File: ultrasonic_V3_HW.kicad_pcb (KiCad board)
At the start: 4 copper layers, 130 x 100 mm, 252 parts, among them J1 71918-140LF, J2 Conn_Coaxial, J3 Conn_Coaxial, J4 Conn_01x07_Pin, J5 Screw_Terminal_01x02, J6 Conn_Coaxial, J7 Conn_Coaxial, Q1 DMN6069SE, Q10 DMN6069SE, Q11 DMN6069SE, Q12 Q_NMOS_GSD, Q2 DMN6069SE, Q3 DMN6069SE, Q4 DMN6069SE, Q5 Q_NMOS_GSD, Q6 Q_NMOS_GSD, Q7 DMN6069SE, Q8 DMN6069SE, Q9 DMN6069SE, U1 MACHXO2-1200HC-4TG100C, U10 MIC4604YM, U11 MIC4604YM, U12 OKI-78SR-3.3_1.5-W36H-C, U13 OKI-78SR-12_1.0-W36H-C, U15 LM34966, U17 OPA388, U18 LM393, U19 TMUX7219, U2 TDC_7200, U20 TMUX7219, U21 TMUX7219, U22 TMUX7219, U23 MCP1501-25xCH, U24 MCP1501-30xCH, U3 MAX9939, U4 TLV3501AID, U5 DAC60501, U6 LM339, U7 ADC10065, U8 MIC4604YM, U9 MIC4604YM, X1 16MHz

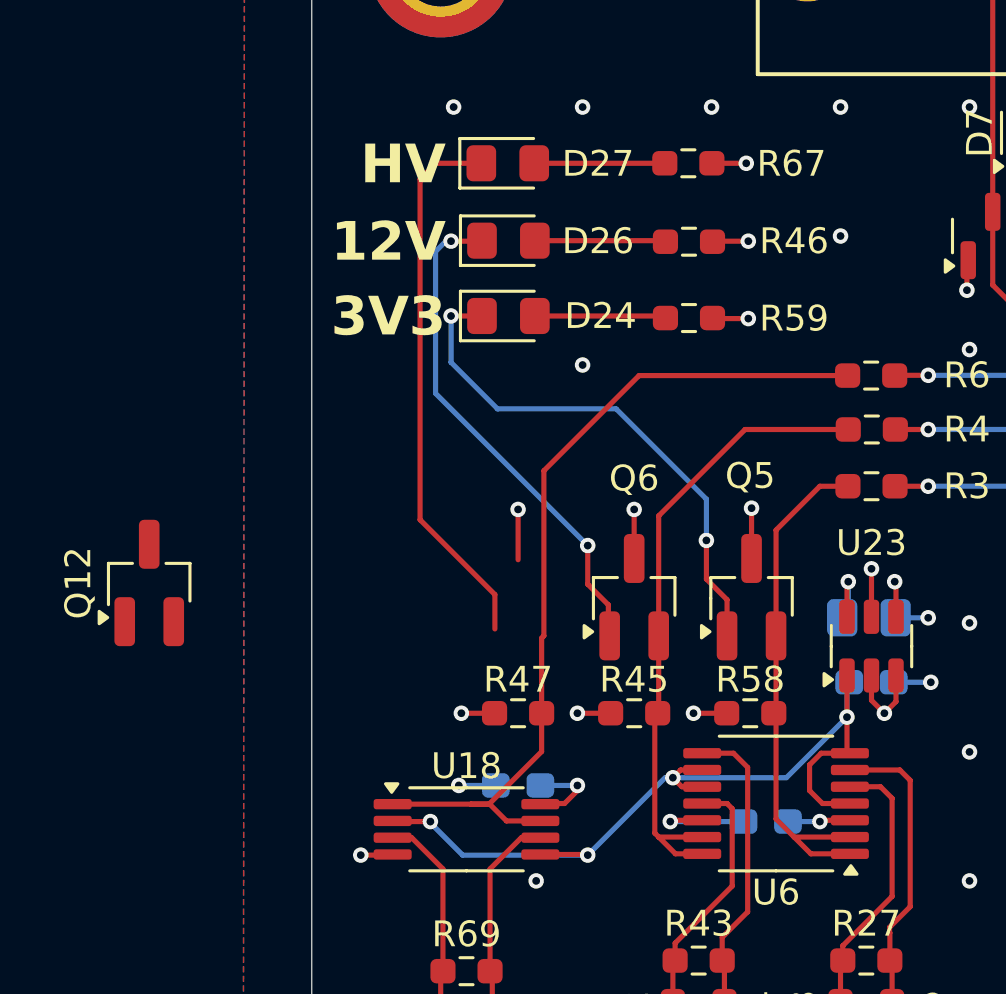
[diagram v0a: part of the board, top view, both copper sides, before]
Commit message: V1 completed, starting on V2 after consultation with mr. Chalupa
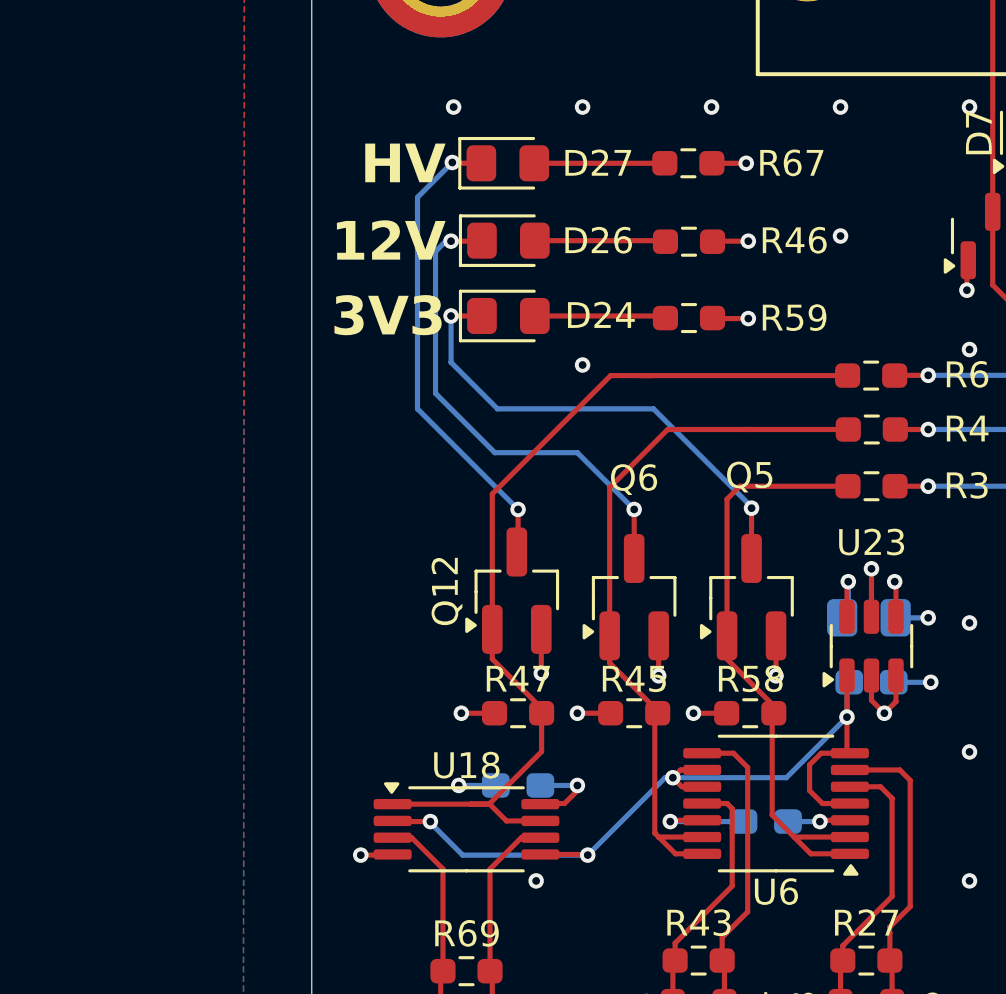
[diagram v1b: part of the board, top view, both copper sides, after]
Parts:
- C3, C34: value C -> 100n
- C35: value C -> 10n
- C36: value C -> 1u
- R62, R63, R64, R65: value R -> 100
- R66: value R -> 6k8
- R71: value R -> 4k7
- moved Q12 14.3 mm to (92.5, 73.8)
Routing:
- net /P_GOOD_P12V: track 25.0 -> 28.5 mm
- net /P_GOOD_P3V3: track 20.3 -> 23.7 mm
- net Net-(D24-K): track 22.4 -> 19.0 mm, vias 3 -> 2
- net GND: track 227.0 -> 229.9 mm, vias 391 -> 393
- net /P_GOOD_PHV: track 33.8 -> 36.5 mm
- net Net-(D27-K): track 21.3 -> 18.7 mm, vias 0 -> 2
- net Net-(D26-K): track 21.3 -> 19.0 mm, vias 3 -> 2

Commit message: V2 finished
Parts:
- removed D10, D11, D12, D13, D15, D8, D9: BAT54S, Package_TO_SOT_SMD:SOT-23
- removed D7: BAT54S, Package_TO_SOT_SMD:SOT-23-3
- removed R85: 12, Resistor_SMD:R_0603_1608Metric
- added C100: 200p, Capacitor_SMD:C_0603_1608Metric_Pad1.08x0.95mm_HandSolder, F.Cu at (185.0, 95.3)
- added C101: 1n, Capacitor_SMD:C_0603_1608Metric_Pad1.08x0.95mm_HandSolder, F.Cu at (158.4, 108.8)
- added C102: 2u2, Capacitor_SMD:C_0805_2012Metric_Pad1.18x1.45mm_HandSolder, F.Cu at (168.8, 107.8)
- added C103: 100n, Capacitor_SMD:C_0603_1608Metric_Pad1.08x0.95mm_HandSolder, F.Cu at (170.7, 107.7)
- added C104: 2u2, Capacitor_SMD:C_0805_2012Metric_Pad1.18x1.45mm_HandSolder, F.Cu at (160.5, 112.7)
- added C105: 100n, Capacitor_SMD:C_0603_1608Metric_Pad1.08x0.95mm_HandSolder, F.Cu at (160.7, 110.5)
- added C106: C, Capacitor_SMD:C_0603_1608Metric_Pad1.08x0.95mm_HandSolder, F.Cu at (169.5, 93.3)
- added C107: C, Capacitor_SMD:C_0603_1608Metric_Pad1.08x0.95mm_HandSolder, F.Cu at (169.5, 94.8)
- added C108: C, Capacitor_SMD:C_0603_1608Metric_Pad1.08x0.95mm_HandSolder, B.Cu at (148.7, 104.6)
- added C109: C, Capacitor_SMD:C_0805_2012Metric_Pad1.18x1.45mm_HandSolder, B.Cu at (145.8, 93.4)
- added C110: 100n, Capacitor_SMD:C_0603_1608Metric_Pad1.08x0.95mm_HandSolder, B.Cu at (164.6, 90.5)
- added C111: C, Capacitor_SMD:C_0603_1608Metric_Pad1.08x0.95mm_HandSolder, B.Cu at (132.3, 84.1)
- added C112: C, Capacitor_SMD:C_0603_1608Metric_Pad1.08x0.95mm_HandSolder, B.Cu at (130.9, 102.3)
- added C113: 100n, Capacitor_SMD:C_0603_1608Metric_Pad1.08x0.95mm_HandSolder, F.Cu at (122.8, 127.2)
- added C114: 10u, Capacitor_SMD:C_0805_2012Metric_Pad1.18x1.45mm_HandSolder, F.Cu at (116.8, 125.3)
- added C115: 10u, Capacitor_SMD:C_0805_2012Metric_Pad1.18x1.45mm_HandSolder, F.Cu at (116.8, 123.3)
- added C116: 100n, Capacitor_SMD:C_0603_1608Metric_Pad1.08x0.95mm_HandSolder, F.Cu at (113.2, 125.6)
- added C117: 100n, Capacitor_SMD:C_0603_1608Metric_Pad1.08x0.95mm_HandSolder, F.Cu at (113.2, 124.1)
- added C118: C, Capacitor_SMD:C_0603_1608Metric_Pad1.08x0.95mm_HandSolder, B.Cu at (181.1, 115.7)
- added C119: C, Capacitor_SMD:C_0603_1608Metric_Pad1.08x0.95mm_HandSolder, B.Cu at (200.8, 114.0)
- added C120: C, Capacitor_SMD:C_0805_2012Metric_Pad1.18x1.45mm_HandSolder, B.Cu at (202.8, 113.8)
- added C121: C, Capacitor_SMD:C_0805_2012Metric_Pad1.18x1.45mm_HandSolder, B.Cu at (183.1, 115.8)
- added C122: C, Capacitor_SMD:C_0603_1608Metric_Pad1.08x0.95mm_HandSolder, B.Cu at (192.7, 72.9)
- added C123: C, Capacitor_SMD:C_0603_1608Metric_Pad1.08x0.95mm_HandSolder, B.Cu at (202.1, 74.7)
- added C124: C, Capacitor_SMD:C_0805_2012Metric_Pad1.18x1.45mm_HandSolder, B.Cu at (191.0, 72.7)
- added C125: C, Capacitor_SMD:C_0805_2012Metric_Pad1.18x1.45mm_HandSolder, B.Cu at (200.1, 74.9)
- added C2: C, Capacitor_SMD:C_0603_1608Metric_Pad1.08x0.95mm_HandSolder, B.Cu at (202.8, 69.5)
- added C90: C, Capacitor_SMD:C_0603_1608Metric_Pad1.08x0.95mm_HandSolder, B.Cu at (203.0, 121.0)
- added C91: C, Capacitor_SMD:C_0805_2012Metric_Pad1.18x1.45mm_HandSolder, B.Cu at (207.0, 119.0)
- added C92: C, Capacitor_SMD:C_0603_1608Metric_Pad1.08x0.95mm_HandSolder, B.Cu at (183.3, 121.0)
- added C93: C, Capacitor_SMD:C_0805_2012Metric_Pad1.18x1.45mm_HandSolder, B.Cu at (187.4, 121.1)
- added C94: 10u, Capacitor_SMD:C_0805_2012Metric_Pad1.18x1.45mm_HandSolder, F.Cu at (122.8, 130.9)
- added C95: 10u, Capacitor_SMD:C_0805_2012Metric_Pad1.18x1.45mm_HandSolder, F.Cu at (120.8, 130.9)
- added C96: 100n, Capacitor_SMD:C_0603_1608Metric_Pad1.08x0.95mm_HandSolder, F.Cu at (120.8, 127.2)
- added C97: 200p, Capacitor_SMD:C_0603_1608Metric_Pad1.08x0.95mm_HandSolder, F.Cu at (188.4, 98.8)
- added C98: 200p, Capacitor_SMD:C_0603_1608Metric_Pad1.08x0.95mm_HandSolder, F.Cu at (188.4, 89.9)
- added C99: 200p, Capacitor_SMD:C_0603_1608Metric_Pad1.08x0.95mm_HandSolder, F.Cu at (185.0, 93.8)
- added D28: SML4740A-E3/61, Diode_SMD:D_SMA_Handsoldering, F.Cu at (105.8, 124.5)
- added FB1: BLM21BD601SN1D, Resistor_SMD:R_0805_2012Metric_Pad1.20x1.40mm_HandSolder, B.Cu at (149.1, 92.4)
- added FB2: BLM21BD601SN1D, Resistor_SMD:R_0805_2012Metric_Pad1.20x1.40mm_HandSolder, B.Cu at (143.9, 85.5)
- added FB3: BLM21BD601SN1D, Resistor_SMD:R_0805_2012Metric_Pad1.20x1.40mm_HandSolder, B.Cu at (131.8, 105.2)
- added FB4: BLM21BD601SN1D, Resistor_SMD:R_0805_2012Metric_Pad1.20x1.40mm_HandSolder, B.Cu at (127.5, 101.4)
- added FB5: BLM21BD601SN1D, Resistor_SMD:R_0805_2012Metric_Pad1.20x1.40mm_HandSolder, B.Cu at (126.5, 95.5)
- added FB6: BLM21BD601SN1D, Resistor_SMD:R_0805_2012Metric_Pad1.20x1.40mm_HandSolder, B.Cu at (127.0, 90.4)
- added Q14: Q_PMOS_DGS, Package_TO_SOT_SMD:SOT-223-3_TabPin2, F.Cu at (105.9, 131.5)
- added R86: 200k, Resistor_SMD:R_0603_1608Metric_Pad0.98x0.95mm_HandSolder, B.Cu at (185.1, 95.3)
- added R87: R, Resistor_SMD:R_0603_1608Metric_Pad0.98x0.95mm_HandSolder, F.Cu at (169.5, 96.3)
- added R88: R, Capacitor_SMD:C_0603_1608Metric_Pad1.08x0.95mm_HandSolder, B.Cu at (143.8, 79.8)
- added U14: THS4521IDGK, Package_SO:VSSOP-8_3.0x3.0mm_P0.65mm, F.Cu at (188.5, 94.4)
- added U25: ADP7142ARDZ-3.3, Package_SO:SOIC-8-1EP_3.9x4.9mm_P1.27mm_EP2.29x3mm, F.Cu at (164.0, 107.0)
- added U26: USBLC6-2SC6, Package_TO_SOT_SMD:SOT-23-6, F.Cu at (122.1, 59.6)
- added U27: USBLC6-2SC6, Package_TO_SOT_SMD:SOT-23-6, F.Cu at (127.1, 59.6)
- added X2: LCMXO-7000HC-6TG-144C, Package_QFP:TQFP-144_20x20mm_P0.5mm, F.Cu at (140.8, 94.5)
- C1: value 100p -> 120p
- C10: value 1u -> C; moved to B.Cu
- C11: value 1u -> C; footprint Capacitor_SMD:C_0603_1608Metric_Pad1.08x0.95mm_HandSolder -> Capacitor_SMD:C_0805_2012Metric_Pad1.18x1.45mm_HandSolder; moved to B.Cu
- C12: value 100p -> 100n
- C14, C19, C23, C78, R83, R84: moved to F.Cu
- C24: value C -> 100p
- C44: footprint Capacitor_SMD:C_0603_1608Metric_Pad1.08x0.95mm_HandSolder -> Capacitor_SMD:C_0805_2012Metric_Pad1.18x1.45mm_HandSolder
- C53, C85: value 1u -> C; footprint Capacitor_SMD:C_0805_2012Metric_Pad1.18x1.45mm_HandSolder -> Capacitor_SMD:C_0603_1608Metric_Pad1.08x0.95mm_HandSolder
- C54: value 100n -> C
- C55: value 10n -> C
- C8: value C -> 120p
- C9: value 100n -> C; footprint Capacitor_SMD:C_0603_1608Metric_Pad1.08x0.95mm_HandSolder -> Capacitor_SMD:C_0805_2012Metric_Pad1.18x1.45mm_HandSolder
- F3, F4, R29: moved to B.Cu
- R14: value R -> 20
- R16: value 1k -> 10
- R17: value 1k -> 100k; footprint Resistor_SMD:R_0603_1608Metric_Pad0.98x0.95mm_HandSolder -> Resistor_SMD:R_1206_3216Metric_Pad1.30x1.75mm_HandSolder
- R18: value 0 -> 200k
- R19: value 1k -> 200k; moved to F.Cu
- R21: value 1k -> 10k; moved to F.Cu
- R23: value R -> 10k
- R60: value R -> 12; footprint Capacitor_SMD:C_0603_1608Metric_Pad1.08x0.95mm_HandSolder -> Resistor_SMD:R_0603_1608Metric; moved to F.Cu
- R7: value 10 -> 20
- R72: value 0 -> 200k; moved to B.Cu
- U1: value MACHXO2-1200HC-4TG100C -> USBLC6-2SC6; footprint Package_QFP:TQFP-100_14x14mm_P0.5mm -> Package_TO_SOT_SMD:SOT-23-6
- U17: value OPA388 -> NE5532; footprint Package_SO:VSSOP-8_3.0x3.0mm_P0.65mm -> Package_SO:SOIC-8_3.9x4.9mm_P1.27mm
- U24: value MCP1501-30xCH -> USBLC6-2SC6
- moved R17 72.3 mm to (101.7, 121.4)
- moved U24 56.1 mm to (111.9, 59.6), turned to -90 degrees
- moved C9 49.9 mm to (207.0, 67.5), turned to -90 degrees
- moved C85 46.1 mm to (138.5, 104.4), turned to 90 degrees
- moved R60 42.8 mm to (126.2, 90.3), turned to 0 degrees
- moved U1 41.5 mm to (117.0, 59.6), turned to -90 degrees
- moved C55 38.9 mm to (140.0, 104.4), turned to 90 degrees
- moved C11 32.8 mm to (187.0, 67.6)
- moved U17 29.5 mm to (196.6, 93.7), turned to 0 degrees
- moved C54 28.5 mm to (150.9, 100.9)
- moved C10 27.3 mm to (182.9, 69.5), turned to -90 degrees
- moved R21 23.4 mm to (192.1, 94.3), turned to 90 degrees
- moved R19 23.4 mm to (188.4, 88.4)
- moved C52 23.0 mm to (150.9, 85.7)
- moved C53 21.1 mm to (150.9, 88.7), turned to 180 degrees
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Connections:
- net Net-(U12-OUT) renamed /PowerManagement/P3V3_UNFUSED
- net Net-(U13-OUT) renamed /PowerManagement/P12V_UNFUSED
- C1 pad 2: Net-(U4-+) -> /AnalogFrontend/AMPLIFIED_SIGNAL_P
- C10 pad 1: Net-(U17A-+) -> /P12V
- C10 pad 2: /AnalogFrontend/AMPLIFIED_SIGNAL_P -> GND
- C11 pad 1: Net-(C11-Pad1) -> GND
- C11 pad 2: GND -> /P12V
- C12 pad 1: /AnalogFrontend/SIGNAL_UNAMPLIFIED_P -> GND
- C12 pad 2: /AnalogFrontend/SIGNAL_UNAMPLIFIED_N -> /P12V
- C13 pad 2: /P3V_REF -> /AnalogFrontend/P3V3_A
- C14 pad 1: /P3V3 -> /AnalogFrontend/P3V3_A
- C15 pad 2: /PHV -> /PowerManagement/step-up/PHV_UNFUSED
- C18 pad 2: /P3V3 -> /AnalogFrontend/P3V3_A
- C19 pad 2: /P3V3 -> /AnalogFrontend/P3V3_A
- C23 pad 2: Net-(U7-VCOM) -> /AnalogFrontend/Vcom
- C24 pad 2: /AnalogFrontend/AMPLIFIED_SIGNAL_P -> Net-(U4--)
- C37 pad 2: /P3V3 -> /fpga/fpgaBankPower/VCCIO0
- C38 pad 1: GND -> /fpga/fpgaBankPower/VCCIO1
- C38 pad 2: /P3V3 -> GND
- C39 pad 1: GND -> /fpga/fpgaBankPower/VCCIO2
- C39 pad 2: /P3V3 -> GND
- C40 pad 1: GND -> /fpga/fpgaBankPower/VCCIO3
- C40 pad 2: /P3V3 -> GND
- C41 pad 2: /P3V3 -> /fpga/fpgaBankPower/VCCIO4
- C42 pad 1: GND -> /fpga/fpgaBankPower/VCCIO5
- C42 pad 2: /P3V3 -> GND
- C43 pad 1: GND -> /fpga/fpgaBankPower/VCCIO0
- C43 pad 2: /P3V3 -> GND
- C44 pad 1: GND -> /P3V3
- C44 pad 2: /P3V3 -> GND
- C45 pad 2: /P3V3 -> /fpga/fpgaBankPower/VCCIO0
- C46 pad 1: GND -> /fpga/fpgaBankPower/VCCIO1
- C46 pad 2: /P3V3 -> GND
- C47 pad 1: GND -> /fpga/fpgaBankPower/VCCIO2
- C47 pad 2: /P3V3 -> GND
- C48 pad 1: GND -> /fpga/fpgaBankPower/VCCIO3
- C48 pad 2: /P3V3 -> GND
- C49 pad 1: GND -> /fpga/fpgaBankPower/VCCIO4
- C49 pad 2: /P3V3 -> GND
- C50 pad 1: GND -> /fpga/fpgaBankPower/VCCIO5
- C50 pad 2: /P3V3 -> GND
- C51 pad 1: GND -> /fpga/fpgaBankPower/VCCIO0
- C51 pad 2: /P3V3 -> GND
- C52 pad 1: GND -> /P3V3
- C52 pad 2: /P3V3 -> GND
- C53 pad 1: GND -> /fpga/fpgaBankPower/VCCIO1
- C53 pad 2: /P3V_REF -> GND
- C54 pad 1: /P3V_REF -> /fpga/fpgaBankPower/VCCIO1
- C55 pad 1: /P3V_REF -> /fpga/fpgaBankPower/VCCIO2
- C62 pad 2: /PHV -> /PowerManagement/step-up/PHV_UNFUSED
- C63 pad 1: /PHV -> /PowerManagement/step-up/PHV_UNFUSED
- C7 pad 2: /P3V3 -> /AnalogFrontend/P3V3_A
- C78 pad 1: /P3V3 -> /AnalogFrontend/P3V3_A
- C85 pad 1: /P3V3 -> /fpga/fpgaBankPower/VCCIO2
- C9 pad 1: /P3V3 -> GND
- C9 pad 2: GND -> /P12V
- F2 pad 1: /PowerManagement/P15V-20V_5S_UNREGULATED -> Net-(D28-K)
- J5 pad 1: /PowerManagement/P15V-20V_5S_UNREGULATED -> GND
- J5 pad 2: GND -> /PowerManagement/P15V-20V_5S_UNREGULATED
- R14 pad 2: Net-(U7-VIN-) -> Net-(U3A-OUTB)
- R15 pad 2: /P3V3 -> /AnalogFrontend/P3V3_A
- R16 pad 1: Net-(R16-Pad1) -> Net-(U4--)
- R16 pad 2: Net-(U17A--) -> /AnalogFrontend/DAC_COMPARATOR_REF
- R17 pad 1: Net-(C11-Pad1) -> GND
- R17 pad 2: Net-(U17A--) -> Net-(D28-A)
- R18 pad 1: /AnalogFrontend/AMPLIFIED_SIGNAL -> Net-(C100-Pad2)
- R18 pad 2: /AnalogFrontend/AMPLIFIED_SIGNAL_P -> /AnalogFrontend/SIGNAL_UNAMPLIFIED_N
- R19 pad 1: /P3V_REF -> Net-(C98-Pad1)
- R19 pad 2: Net-(U17A-+) -> /AnalogFrontend/SIGNAL_UNAMPLIFIED_P
- R21 pad 1: Net-(U17A-+) -> /AnalogFrontend/P3V3_A
- R21 pad 2: GND -> Net-(U17A-+)
- R22 pad 2: /P3V3 -> /AnalogFrontend/P3V3_A
- R23 pad 1: /AnalogFrontend/AMPLIFIED_SIGNAL_P -> Net-(U17A-+)
- R23 pad 2: Net-(U7-VIN+) -> GND
- R25 pad 1: Net-(U7-VCOM) -> Net-(U7-VIN+)
- R25 pad 2: Net-(U7-VIN-) -> /AnalogFrontend/Vcom
- R29 pad 2: Net-(U4-+) -> /AnalogFrontend/AMPLIFIED_SIGNAL_N
- R5 pad 1: /AnalogFrontend/AMPLIFIED_SIGNAL_P -> Net-(U3A-OUTA)
- R60 pad 1: /P3V3 -> /SPI_LOCAL_MISO
- R60 pad 2: /CNTRL_GPIO2 -> Net-(X2F-PL8B)
- R62 pad 1: /LVDS_SCLK_P -> /fpga/LVDS_SCLK_TVS_N
- R62 pad 2: /LVDS_SCLK_N -> /fpga/LVDS_SCLK_TVS_P
- R63 pad 1: /LVDS_CS_P -> /fpga/LVDS_CS_TVS_P
- R63 pad 2: /LVDS_CS_N -> /fpga/LVDS_CS_TVS_N
- R64 pad 1: /LVDS_MISO_P -> /fpga/LVDS_MISO_TVS_P
- R64 pad 2: /LVDS_MISO_N -> /fpga/LVDS_MISO_TVS_N
- R65 pad 1: /LVDS_MOSI_P -> /fpga/LVDS_MOSI_TVS_P
- R65 pad 2: /LVDS_MOSI_N -> /fpga/LVDS_MOSI_TVS_N
- R7 pad 1: Net-(U4-+) -> /AnalogFrontend/AMPLIFIED_SIGNAL_P
- R7 pad 2: /AnalogFrontend/AMPLIFIED_SIGNAL -> Net-(U3A-OUTA)
- R72 pad 1: /AnalogFrontend/AMPLIFIED_SIGNAL -> Net-(C98-Pad1)
- R72 pad 2: Net-(R16-Pad1) -> /AnalogFrontend/HALF_VDDA
- R8 pad 2: /AnalogFrontend/AMPLIFIED_SIGNAL_N -> Net-(U3A-OUTB)
- R83 pad 1: /SPI_LOCAL_MISO -> /SPI_LOCAL_SCK
- R83 pad 2: Net-(U1D-PL4A) -> Net-(X2F-PL6A/PCLKT5_0)
- R84 pad 2: Net-(U1D-PL4B) -> Net-(X2F-PL9B)
- U1 pad 1: /fpga/CLK -> /LVDS_CS_N
- U1 pad 2: unconnected-(U1D-PL2D/L_GPLLC_IN-Pad2) -> GND
- U1 pad 3: unconnected-(U1D-PL3A/PCLKT3_2-Pad3) -> /LVDS_CS_P
- U1 pad 4: unconnected-(U1D-PL3B/PCLKC3_2-Pad4) -> /fpga/LVDS_CS_TVS_P
- U1 pad 6: GND -> /fpga/LVDS_CS_TVS_N
- U17 pad 1: unconnected-(U17B-NC-Pad1) -> /AnalogFrontend/HALF_VDDA
- U17 pad 2: Net-(U17A--) -> /AnalogFrontend/HALF_VDDA
- U17 pad 6: Net-(R16-Pad1) -> unconnected-(U17B---Pad6)
- U17 pad 7: /P3V3 -> unconnected-(U17-Pad7)
- U17 pad 8: unconnected-(U17B-NC-Pad8) -> /P12V
- U2 pad 5: /fpga/CLK -> /fpga/TDC_CLK
- U20 pad 8: /AnalogFrontend/SIGNAL_UNAMPLIFIED_P -> /AnalogFrontend/SIGNAL_UNAMPLIFIED_N
- U22 pad 8: /AnalogFrontend/SIGNAL_UNAMPLIFIED_N -> /AnalogFrontend/SIGNAL_UNAMPLIFIED_P
- U24 pad 1: /P3V_REF -> /LVDS_SCLK_N
- U24 pad 3: GND -> /LVDS_SCLK_P
- U24 pad 4: /P3V3 -> /fpga/LVDS_SCLK_TVS_P
- U24 pad 5: GND -> /P3V3
- U24 pad 6: /P3V3 -> /fpga/LVDS_SCLK_TVS_N
- U3 pad 4: /AnalogFrontend/SIGNAL_UNAMPLIFIED_N -> Net-(U3A-INA-)
- U3 pad 5: /AnalogFrontend/SIGNAL_UNAMPLIFIED_P -> Net-(U3A-INA+)
- U3 pad 6: /AnalogFrontend/AMPLIFIED_SIGNAL_N -> Net-(U3A-OUTB)
- U3 pad 8: /AnalogFrontend/AMPLIFIED_SIGNAL_P -> Net-(U3A-OUTA)
- U3 pad 9: /P3V3 -> /AnalogFrontend/P3V3_A
- U4 pad 2: /AnalogFrontend/DAC_COMPARATOR_REF -> Net-(U4--)
- U4 pad 3: Net-(U4-+) -> /AnalogFrontend/AMPLIFIED_SIGNAL_N
- U4 pad 7: /P3V3 -> /AnalogFrontend/P3V3_A
- U5 pad 1: /P3V3 -> /AnalogFrontend/P3V3_A
- U5 pad 10: /P3V_REF -> /AnalogFrontend/P3V3_A
- U7 pad 10: /P3V3 -> /AnalogFrontend/P3V3_A
- U7 pad 2: /P3V3 -> /AnalogFrontend/P3V3_A
- U7 pad 4: Net-(U7-VCOM) -> /AnalogFrontend/Vcom
- U7 pad 9: /P3V3 -> /AnalogFrontend/P3V3_A
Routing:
- net /P12V: track 259.1 -> 122.6 mm, vias 8 -> 19
- net /P3V3: track 168.4 -> 70.4 mm, vias 73 -> 37
- net /AnalogFrontend/P3V3_A: track 0.00 -> 66.6 mm, vias 0 -> 9
- net /CHARGE_AMP_SHT: track 0.00 -> 59.1 mm, vias 0 -> 2
- net /ADC_DF: track 55.6 -> 8.80 mm, vias 2 -> 0
- net /LVDS_SCLK_P: track 51.2 -> 11.3 mm
- net /LVDS_SCLK_N: track 46.6 -> 8.56 mm
- net /LVDS_MISO_P: track 48.6 -> 11.3 mm
- net /LVDS_CS_P: track 48.2 -> 11.3 mm
- net /P3V_REF: track 35.7 -> 0.00 mm, vias 2 -> 0
- net /LVDS_MOSI_P: track 37.5 -> 1.74 mm
- net /fpga/LVDS_SCLK_TVS_P: track 0.00 -> 35.7 mm
- net /fpga/LVDS_SCLK_TVS_N: track 0.00 -> 35.7 mm
- net /LVDS_MISO_N: track 44.1 -> 8.55 mm
- net /LVDS_CS_N: track 43.6 -> 8.56 mm
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- added copper zone on F.Cu, net /AnalogFrontend/P3V3_A
- added copper zone on B.Cu, net /P12V
- added copper zone on F.Cu, net /P12V
- added copper zone on B.Cu, net /PowerManagement/P12V_UNFUSED
- added copper zone on B.Cu, net /PowerManagement/P3V3_UNFUSED
- added copper zone on B.Cu, net /fpga/fpgaBankPower/VCCIO0
- added copper zone on B.Cu, net /fpga/fpgaBankPower/VCCIO1
- added copper zone on B.Cu, net /fpga/fpgaBankPower/VCCIO2
- added copper zone on B.Cu, net /fpga/fpgaBankPower/VCCIO3
- added copper zone on B.Cu, net /fpga/fpgaBankPower/VCCIO4
- added copper zone on B.Cu, net /fpga/fpgaBankPower/VCCIO5
- removed copper zone on F.Cu, net /P3V3
- removed copper zone on In2.Cu, net /P3V3
